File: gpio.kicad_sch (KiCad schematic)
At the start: 30 parts, among them Q1 AUIRF7316QTR, Q2 AUIRF7316QTR, Q3 AUIRF7316QTR, Q4 AUIRF7316QTR, U4 NPIC6C596ADJ, U5 PCF8574DWR

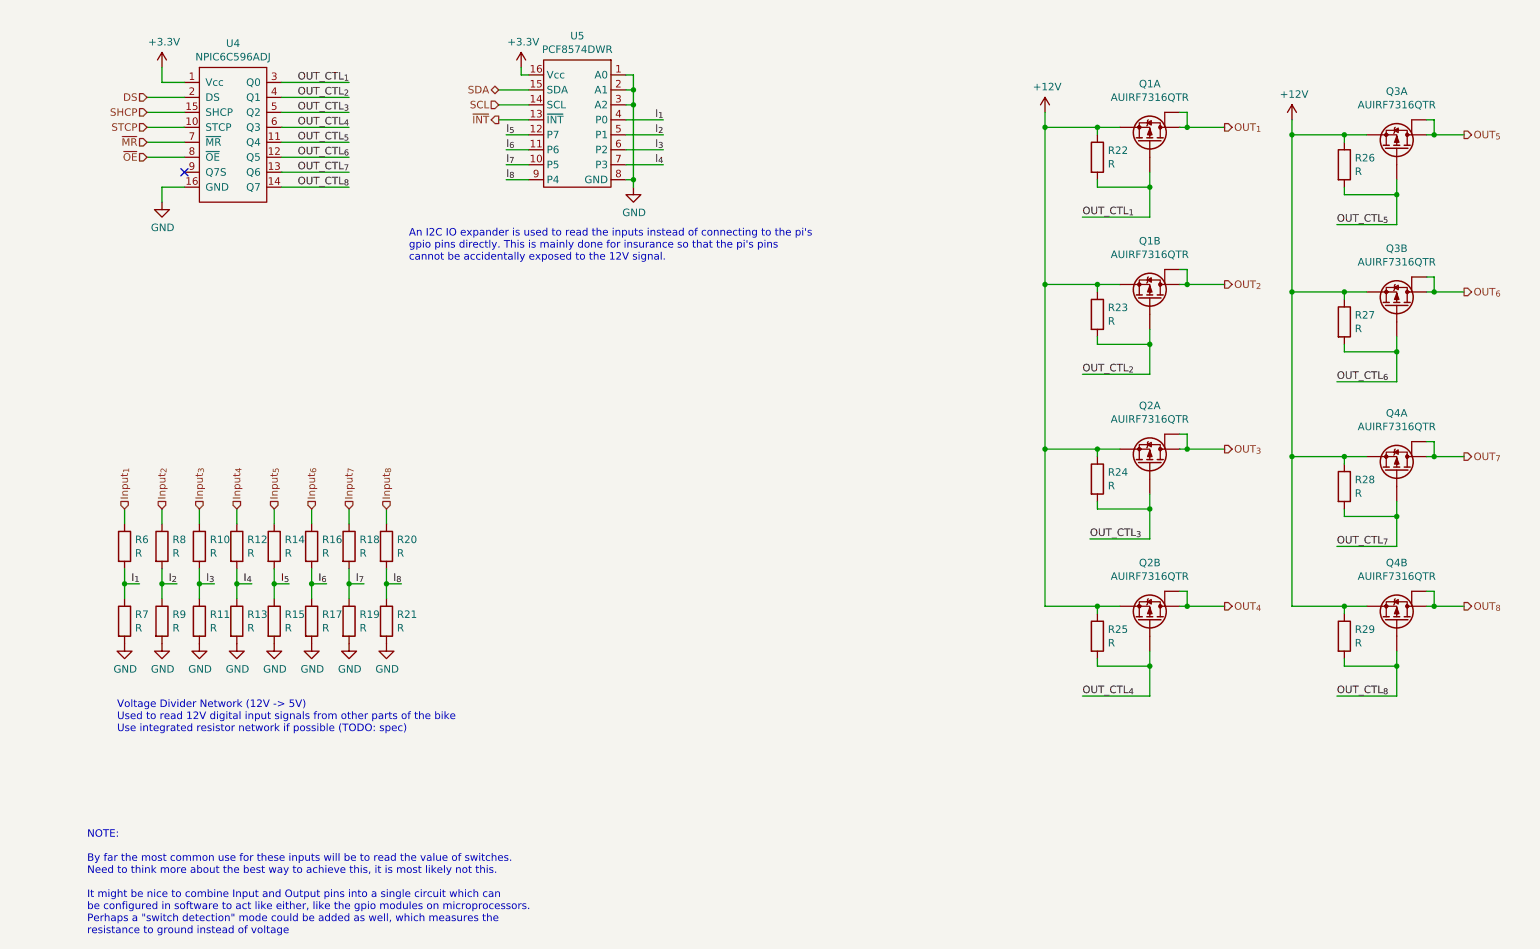
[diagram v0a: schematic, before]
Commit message: Added buses and USB ports to schematic
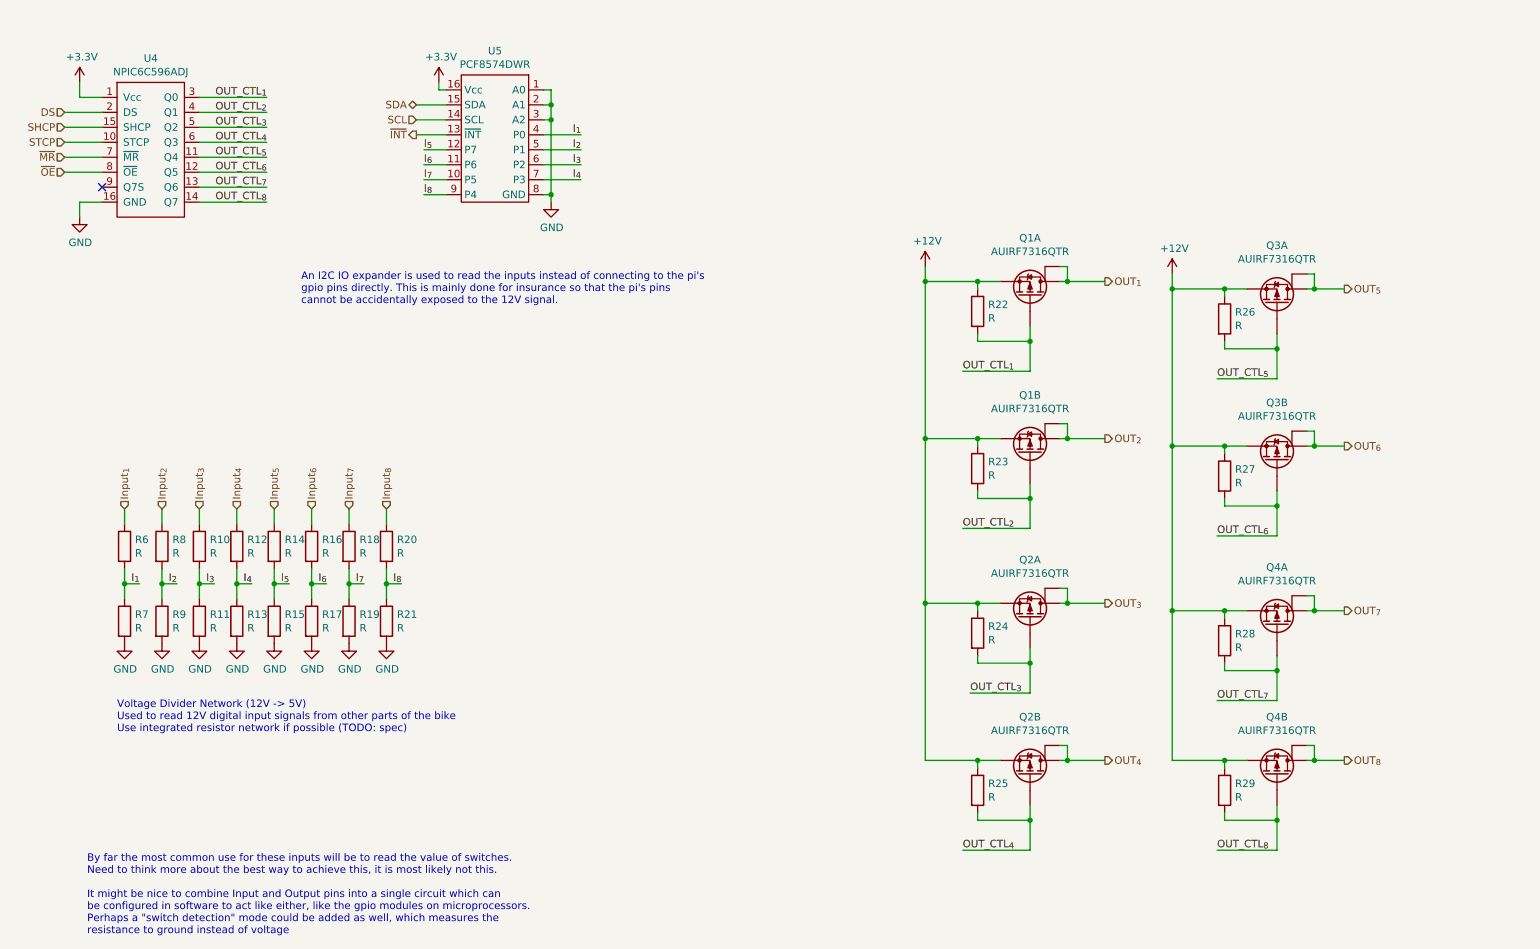
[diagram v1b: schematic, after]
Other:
- note added: "By far the most common use for these inputs will be to read the value of switches. Need to think more about the best way to achieve this, it is most likely not this. It might be nice to combine Input and Output pins into a single circuit which can be configured in software to act like either, like the gpio modules on microprocessors. Perhaps a "switch detection" mode could be added as well, which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"
- note removed: "NOTE: By far the most common use for these inputs will be to read the value of switches. Need to think more about the best way to achieve this, it is most likely not this. It might be nice to combine Input and Output pins into a single circuit which can be configured in software to act like either, like the gpio modules on microprocessors. Perhaps a "switch detection" mode could be added as well,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"
- company: (none) -> eCafe Racer
- title: (none) -> Dennis
- moved on the sheet: Q1A, Q1B, Q2A, Q2B, Q3A, Q3B, Q4A, Q4B, R22, R23, R24, R25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

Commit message: footprints
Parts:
- R15: renamed from R6; footprint (none) -> Resistor_SMD:R_0805_2012Metric
- R16: renamed from R7; footprint (none) -> Resistor_SMD:R_0805_2012Metric
- R17: renamed from R8; footprint (none) -> Resistor_SMD:R_0805_2012Metric
- R18: renamed from R9; footprint (none) -> Resistor_SMD:R_0805_2012Metric
- R19: renamed from R10; footprint (none) -> Resistor_SMD:R_0805_2012Metric
- R20: renamed from R11; footprint (none) -> Resistor_SMD:R_0805_2012Metric
- R21: renamed from R12; footprint (none) -> Resistor_SMD:R_0805_2012Metric
- R22: renamed from R13; footprint (none) -> Resistor_SMD:R_0805_2012Metric
- R23: renamed from R14; footprint (none) -> Resistor_SMD:R_0805_2012Metric
- R24: renamed from R15; footprint (none) -> Resistor_SMD:R_0805_2012Metric
- R25: renamed from R16; footprint (none) -> Resistor_SMD:R_0805_2012Metric
- R26: renamed from R17; footprint (none) -> Resistor_SMD:R_0805_2012Metric
- R27: renamed from R18; footprint (none) -> Resistor_SMD:R_0805_2012Metric
- R28: renamed from R19; footprint (none) -> Resistor_SMD:R_0805_2012Metric
- R29: renamed from R20; footprint (none) -> Resistor_SMD:R_0805_2012Metric
- R30: renamed from R21; footprint (none) -> Resistor_SMD:R_0805_2012Metric
- R31: renamed from R22; footprint (none) -> Resistor_SMD:R_0805_2012Metric
- R32: renamed from R23; footprint (none) -> Resistor_SMD:R_0805_2012Metric
- R33: renamed from R24; footprint (none) -> Resistor_SMD:R_0805_2012Metric
- R34: renamed from R25; footprint (none) -> Resistor_SMD:R_0805_2012Metric
- R35: renamed from R26; footprint (none) -> TestPoint:TestPoint_2Pads_Pitch2.54mm_Drill0.8mm
- R36: renamed from R27; footprint (none) -> Resistor_SMD:R_0805_2012Metric
- R37: renamed from R28; footprint (none) -> Resistor_SMD:R_0805_2012Metric
- R38: renamed from R29; footprint (none) -> Resistor_SMD:R_0805_2012Metric
- renumbered U4 to U5, U5 to U6

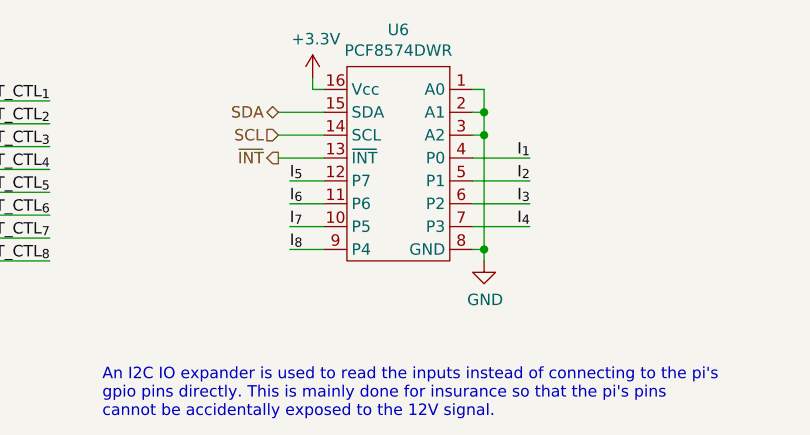
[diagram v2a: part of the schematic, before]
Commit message: footprint assignments
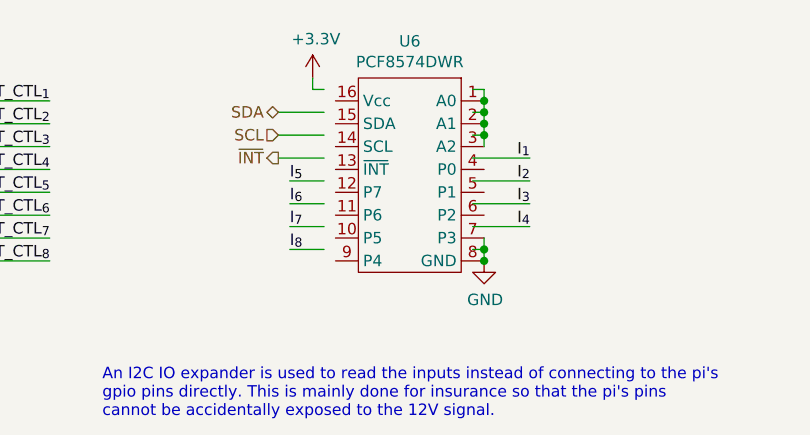
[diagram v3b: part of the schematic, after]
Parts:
- U6: footprint (none) -> Package_SO:SOIC-16W_7.5x10.3mm_P1.27mm
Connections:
- net +3V3: no longer U6.16 (Vcc)
- net GND: now also U6.7 (P3); no longer U6.1 (A0), U6.2 (A1), U6.3 (A2)
- net I_{1}: no longer U6.4 (P0)
- net I_{2}: no longer U6.5 (P1)
- net I_{3}: no longer U6.6 (P2)
- net I_{4}: no longer U6.7 (P3)
- net I_{5}: no longer U6.12 (P7)
- net I_{6}: no longer U6.11 (P6)
- net I_{7}: no longer U6.10 (P5)
- net I_{8}: no longer U6.9 (P4)
- net SCL: no longer U6.14 (SCL)
- net SDA: no longer U6.15 (SDA)
- net ~INT: no longer U6.13 (~INT)
- new net: U6.1 (A0), U6.2 (A1), U6.3 (A2)
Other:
- moved on the sheet: U6
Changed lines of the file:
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@@
   (junction (at 81.28 119.38) (diameter 0.9144) (color 0 0 0 0))
   (junction (at 87.63 119.38) (diameter 0.9144) (color 0 0 0 0))
+  (junction (at 115.57 36.83) (diameter 0.9144) (color 0 0 0 0))
   (junction (at 115.57 38.1) (diameter 0.9144) (color 0 0 0 0))
+  (junction (at 115.57 39.37) (diameter 0.9144) (color 0 0 0 0))
   (junction (at 115.57 40.64) (diameter 0.9144) (color 0 0 0 0))
   (junction (at 115.57 53.34) (diameter 0.9144) (color 0 0 0 0))
+  (junction (at 115.57 54.61) (diameter 0.9144) (color 0 0 0 0))
   (junction (at 179.07 68.072) (diameter 0.9144) (color 0 0 0 0))
   (junction (at 179.07 94.742) (diameter 0.9144) (color 0 0 0 0))
@@
     (stroke (width 0) (type solid) (color 0 0 0 0))
   )
-  (wire (pts (xy 115.57 38.1) (xy 115.57 35.56))
-    (stroke (width 0) (type solid) (color 0 0 0 0))
-  )
-  (wire (pts (xy 115.57 40.64) (xy 115.57 38.1))
-    (stroke (width 0) (type solid) (color 0 0 0 0))
-  )
-  (wire (pts (xy 115.57 53.34) (xy 115.57 40.64))
+  (wire (pts (xy 115.57 36.83) (xy 115.57 35.56))
+    (stroke (width 0) (type solid) (color 0 0 0 0))
+  )
+  (wire (pts (xy 115.57 38.1) (xy 115.57 36.83))
+    (stroke (width 0) (type solid) (color 0 0 0 0))
+  )
+  (wire (pts (xy 115.57 39.37) (xy 115.57 38.1))
+    (stroke (width 0) (type solid) (color 0 0 0 0))
+  )
+  (wire (pts (xy 115.57 40.64) (xy 115.57 39.37))
+    (stroke (width 0) (type solid) (color 0 0 0 0))
+  )
+  (wire (pts (xy 115.57 41.91) (xy 115.57 40.64))
+    (stroke (width 0) (type solid) (color 0 0 0 0))
+  )
+  (wire (pts (xy 115.57 53.34) (xy 115.57 52.07))
     (stroke (width 0) (type solid) (color 0 0 0 0))
   )
@@
   (symbol (lib_id "power:+3.3V") (at 35.56 34.29 0) (unit 1)
     (in_bom yes) (on_board yes)
-    (property "Reference" "#PWR0144" (id 0) (at 35.56 38.1 0)
+    (property "Reference" "#PWR0140" (id 0) (at 35.56 38.1 0)
       (effects (font (size 1.27 1.27)) hide)
     )
@@
   (symbol (lib_id "power:+3.3V") (at 96.52 34.29 0) (unit 1)
     (in_bom yes) (on_board yes)
-    (property "Reference" "#PWR0137" (id 0) (at 96.52 38.1 0)
+    (property "Reference" "#PWR0146" (id 0) (at 96.52 38.1 0)
       (effects (font (size 1.27 1.27)) hide)
     )
@@
   (symbol (lib_id "power:+12V") (at 179.07 65.532 0) (unit 1)
     (in_bom yes) (on_board yes)
-    (property "Reference" "#PWR0139" (id 0) (at 179.07 69.342 0)
+    (property "Reference" "#PWR0152" (id 0) (at 179.07 69.342 0)
       (effects (font (size 1.27 1.27)) hide)
     )
@@
   (symbol (lib_id "power:+12V") (at 220.98 66.802 0) (unit 1)
     (in_bom yes) (on_board yes)
-    (property "Reference" "#PWR0136" (id 0) (at 220.98 70.612 0)
+    (property "Reference" "#PWR0153" (id 0) (at 220.98 70.612 0)
       (effects (font (size 1.27 1.27)) hide)
     )
@@
   (symbol (lib_id "power:GND") (at 35.56 57.15 0) (unit 1)
     (in_bom yes) (on_board yes)
-    (property "Reference" "#PWR0143" (id 0) (at 35.56 63.5 0)
+    (property "Reference" "#PWR0141" (id 0) (at 35.56 63.5 0)
       (effects (font (size 1.27 1.27)) hide)
     )
@@
   (symbol (lib_id "power:GND") (at 43.18 129.54 0) (unit 1)
     (in_bom yes) (on_board yes)
-    (property "Reference" "#PWR0141" (id 0) (at 43.18 135.89 0)
+    (property "Reference" "#PWR0144" (id 0) (at 43.18 135.89 0)
       (effects (font (size 1.27 1.27)) hide)
     )
@@
   (symbol (lib_id "power:GND") (at 55.88 129.54 0) (unit 1)
     (in_bom yes) (on_board yes)
-    (property "Reference" "#PWR0140" (id 0) (at 55.88 135.89 0)
+    (property "Reference" "#PWR0143" (id 0) (at 55.88 135.89 0)
       (effects (font (size 1.27 1.27)) hide)
     )
@@
   (symbol (lib_id "power:GND") (at 62.23 129.54 0) (unit 1)
     (in_bom yes) (on_board yes)
-    (property "Reference" "#PWR0145" (id 0) (at 62.23 135.89 0)
+    (property "Reference" "#PWR0151" (id 0) (at 62.23 135.89 0)
       (effects (font (size 1.27 1.27)) hide)
     )
@@
   (symbol (lib_id "power:GND") (at 68.58 129.54 0) (unit 1)
     (in_bom yes) (on_board yes)
-    (property "Reference" "#PWR0146" (id 0) (at 68.58 135.89 0)
+    (property "Reference" "#PWR0150" (id 0) (at 68.58 135.89 0)
       (effects (font (size 1.27 1.27)) hide)
     )
@@
   (symbol (lib_id "power:GND") (at 74.93 129.54 0) (unit 1)
     (in_bom yes) (on_board yes)
-    (property "Reference" "#PWR0149" (id 0) (at 74.93 135.89 0)
+    (property "Reference" "#PWR0148" (id 0) (at 74.93 135.89 0)
       (effects (font (size 1.27 1.27)) hide)
     )
@@
   (symbol (lib_id "power:GND") (at 81.28 129.54 0) (unit 1)
     (in_bom yes) (on_board yes)
-    (property "Reference" "#PWR0148" (id 0) (at 81.28 135.89 0)
+    (property "Reference" "#PWR0149" (id 0) (at 81.28 135.89 0)
       (effects (font (size 1.27 1.27)) hide)
     )
@@
   (symbol (lib_id "power:GND") (at 115.57 54.61 0) (unit 1)
     (in_bom yes) (on_board yes)
-    (property "Reference" "#PWR0138" (id 0) (at 115.57 60.96 0)
+    (property "Reference" "#PWR0145" (id 0) (at 115.57 60.96 0)
       (effects (font (size 1.27 1.27)) hide)
     )
@@
     )
   )
-  (symbol (lib_id "symbols:PCF8574DWR") (at 106.68 44.45 0) (mirror y) (unit 1)
-    (in_bom yes) (on_board yes)
-    (property "Reference" "U6" (id 0) (at 106.045 28.9365 0))
-    (property "Value" "PCF8574DWR" (id 1) (at 106.045 31.2352 0))
-    (property "Footprint" "" (id 2) (at 110.49 30.48 0)
-      (effects (font (size 1.27 1.27)) hide)
-    )
-    (property "Datasheet" "https://www.ti.com/lit/ds/symlink/pcf8574.pdf?HQS=dis-dk-null-digikeymode-dsf-pf-null-wwe&ts=1609224079098" (id 3) (at 110.49 30.48 0)
-      (effects (font (size 1.27 1.27)) hide)
-    )
-    (property "Vendor" "Digikey" (id 4) (at 106.68 44.45 0)
-      (effects (font (size 1.27 1.27)) hide)
-    )
-    (property "Vendor Part" "296-13108-1-ND" (id 5) (at 106.68 44.45 0)
-      (effects (font (size 1.27 1.27)) hide)
-    )
-    (property "Manufacturer" "Texas Instruments" (id 6) (at 106.68 44.45 0)
-      (effects (font (size 1.27 1.27)) hide)
-    )
-    (property "Manufacturer Part" "PCF8574DWR" (id 7) (at 106.68 44.45 0)
-      (effects (font (size 1.27 1.27)) hide)
-    )
+  (symbol (lib_id "symbols:PCF8574DWR") (at 107.95 45.72 0) (mirror y) (unit 1)
+    (in_bom yes) (on_board yes)
+    (property "Reference" "U6" (id 0) (at 107.315 30.2065 0))
+    (property "Value" "PCF8574DWR" (id 1) (at 107.315 32.5052 0))
+    (property "Footprint" "Package_SO:SOIC-16W_7.5x10.3mm_P1.27mm" (id 2) (at 111.76 31.75 0)
+      (effects (font (size 1.27 1.27)) hide)
+    )
+    (property "Datasheet" "https://www.ti.com/lit/ds/symlink/pcf8574.pdf?HQS=dis-dk-null-digikeymode-dsf-pf-null-wwe&ts=1609224079098" (id 3) (at 111.76 31.75 0)
+      (effects (font (size 1.27 1.27)) hide)
+    )
+    (property "Vendor" "Digikey" (id 4) (at 107.95 45.72 0)
+      (effects (font (size 1.27 1.27)) hide)
+    )
+    (property "Vendor Part" "296-13108-1-ND" (id 5) (at 107.95 45.72 0)
+      (effects (font (size 1.27 1.27)) hide)
+    )
+    (property "Manufacturer" "Texas Instruments" (id 6) (at 107.95 45.72 0)
+      (effects (font (size 1.27 1.27)) hide)
+    )
+    (property "Manufacturer Part" "PCF8574DWR" (id 7) (at 107.95 45.72 0)
+      (effects (font (size 1.27 1.27)) hide)
+    )
